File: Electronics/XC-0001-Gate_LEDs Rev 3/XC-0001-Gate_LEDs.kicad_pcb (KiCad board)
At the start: 2 copper layers, 76 x 60 mm, 16 parts, among them J1 DC12V_IN, J2 BuckBlock_NP, J3 LED_DIM, J4 LED_NODIM, J5 AC_IN, J6 AC_OUT

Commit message: Version 2 updates
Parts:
- removed JP1: Squelch_NO, Connector_Wire:SolderWire-0.25sqmm_1x02_P4.2mm_D0.65mm_OD1.7mm
- added C1: 22µF, Capacitor_SMD:C_1206_3216Metric_Pad1.33x1.80mm_HandSolder, B.Cu at (142.0, 121.0)
- added C2: 4.8µF, Capacitor_SMD:C_1206_3216Metric_Pad1.33x1.80mm_HandSolder, F.Cu at (147.8, 106.5)
- added C3: 10µF, Capacitor_SMD:C_1206_3216Metric_Pad1.33x1.80mm_HandSolder, F.Cu at (144.0, 106.5)
- added J7: Dim_Select, Connector_PinHeader_2.54mm:PinHeader_1x04_P2.54mm_Vertical, F.Cu at (138.0, 117.7)
- added L1: 68µH, Inductor_THT:L_Radial_D9.5mm_P5.00mm_Fastron_07HVP, F.Cu at (132.5, 102.0)
- added U1: LDU1416S1000, XC-footprint-lib:LDU1416S1000, F.Cu at (140.7, 93.0)
- J1, J3, J4: footprint Connector_Wire:SolderWire-0.25sqmm_1x02_P4.2mm_D0.65mm_OD1.7mm -> Connector_Wire:SolderWire-1.5sqmm_1x02_P7.8mm_D1.7mm_OD3.9mm
- J2: value BuckBlock_NP -> Driver_Ext; footprint Connector_Wire:SolderWire-1sqmm_1x06_P7.8mm_D1.4mm_OD3.9mm -> XC-footprint-lib:SolderWire-1.5sqmm_1x06_Grouped2x3_P6mm_D1.7mm_OD3mm
- J5, J6: footprint Connector_Wire:SolderWire-0.75sqmm_1x02_P7mm_D1.25mm_OD3.5mm -> Connector_Wire:SolderWire-1.5sqmm_1x02_P7.8mm_D1.7mm_OD3.9mm
- moved J2 24.8 mm to (164.5, 115.5)
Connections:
- net +12V renamed DC+12V
- net /LED+ renamed /DIM+
- net /LED- renamed /DIM-
- J2 pad 2: /DIM_ANALOG -> /DIM_CTRL
- RV1 pad 2: /DIM_ANALOG -> Net-(J7-Pad4)
- RV1 pad 3: /DIM_ANALOG -> Net-(J7-Pad4)
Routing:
- net /DIM_CTRL: track 0.00 -> 57.1 mm
- net /DIM+: track 19.8 -> 55.0 mm
- net /DIM-: track 8.24 -> 42.0 mm
- net /DIM_ANALOG: track 30.4 -> 0.00 mm
- net /DIM_GND: track 36.9 -> 54.9 mm
- net Net-(J7-Pad4): track 0.00 -> 16.5 mm
- net DC+12V: track 49.9 -> 64.9 mm, vias 0 -> 1
- net NEUT: track 26.0 -> 27.7 mm
- net DC-12V: vias 77 -> 112
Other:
- board size 76 x 60 mm -> 92 x 60 mm
- net class AC removed
- net class DC Pwr removed
- net class Default removed
- board text added: "+12V"
- board text added: "DIM"
- board text added: "Dim Pot"
- board text added: "Ext. Driver"
- board text added: "J7 Dim_Select Jumper: 4+3 → RV1 dimmer control 3+2 → Squelch (Full Dim) 2+1 → Disable (No Dim)"
- board text added: "Out"
- board text added: "Power"
- board text added: "RAC01-12SGB"
- board text added: "RV1 Dim Pot: A009 Offboard → 20KΩ LDU14 Onboard → 2MΩ"
- board text added: "XC-0001 Gate LED Control 3 04-2021"
- board text removed: "BuckBlock A009"
- board text removed: "Dim"
- board text removed: "Squelch (NO)"
- board text removed: "XC-0001 Gate LED Control 2 03-2021"

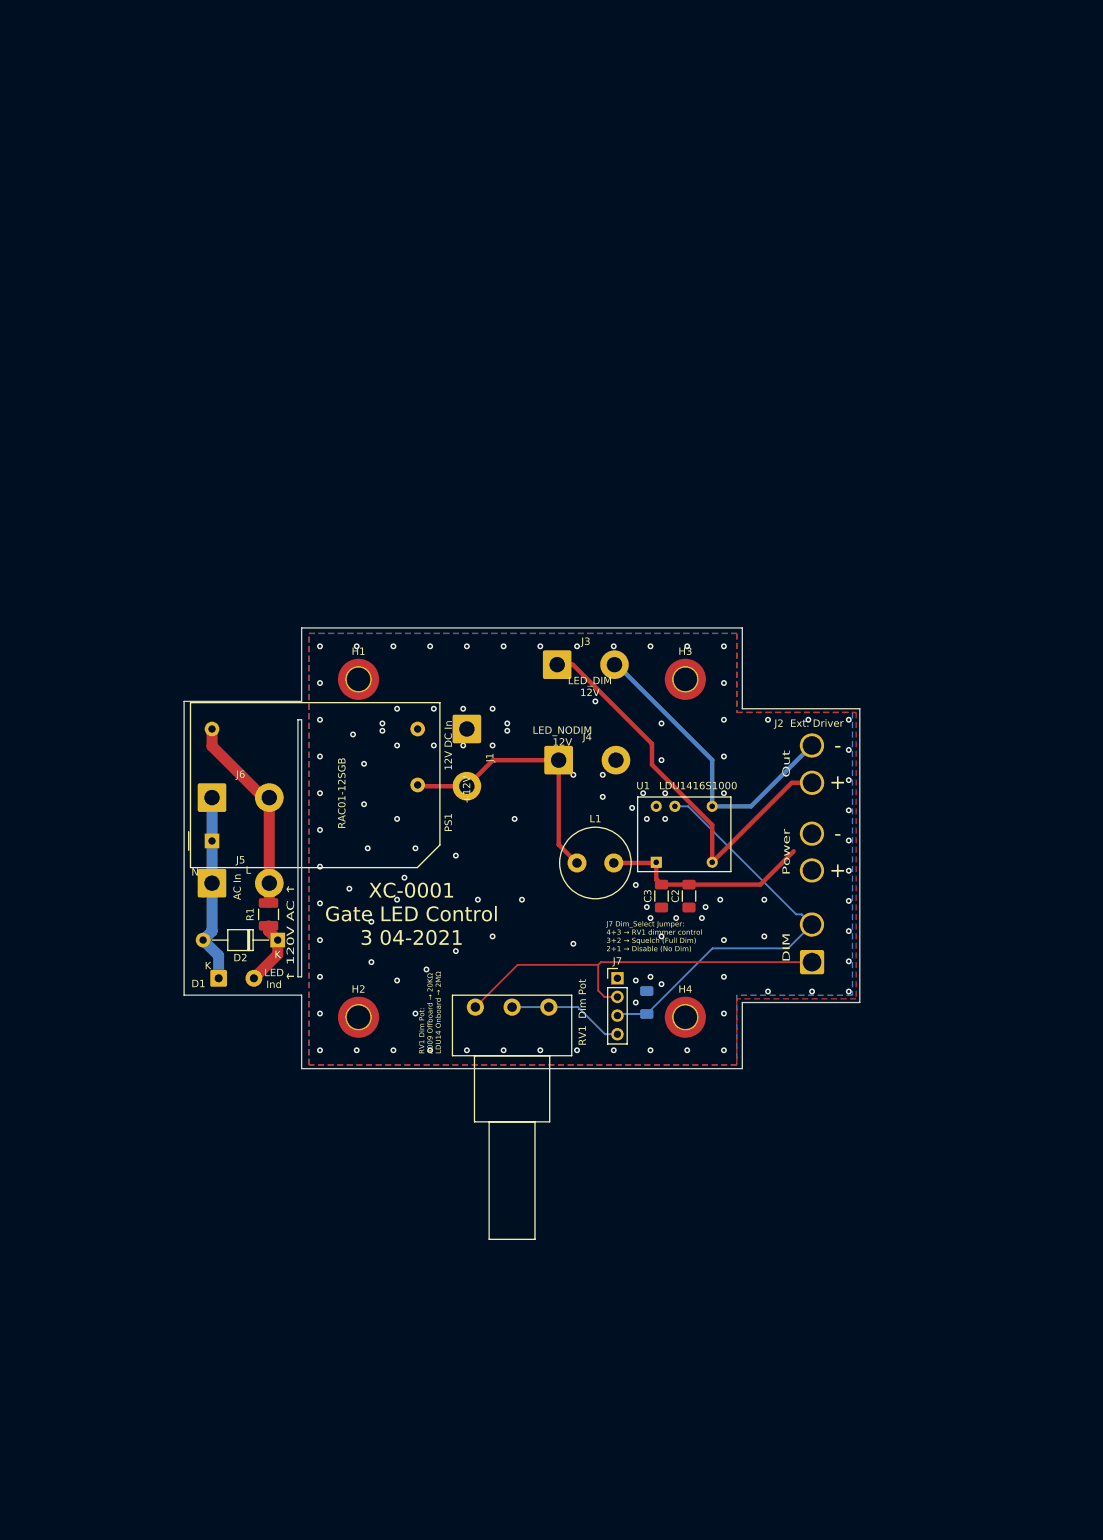
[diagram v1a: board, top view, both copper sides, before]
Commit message: Ignore backup
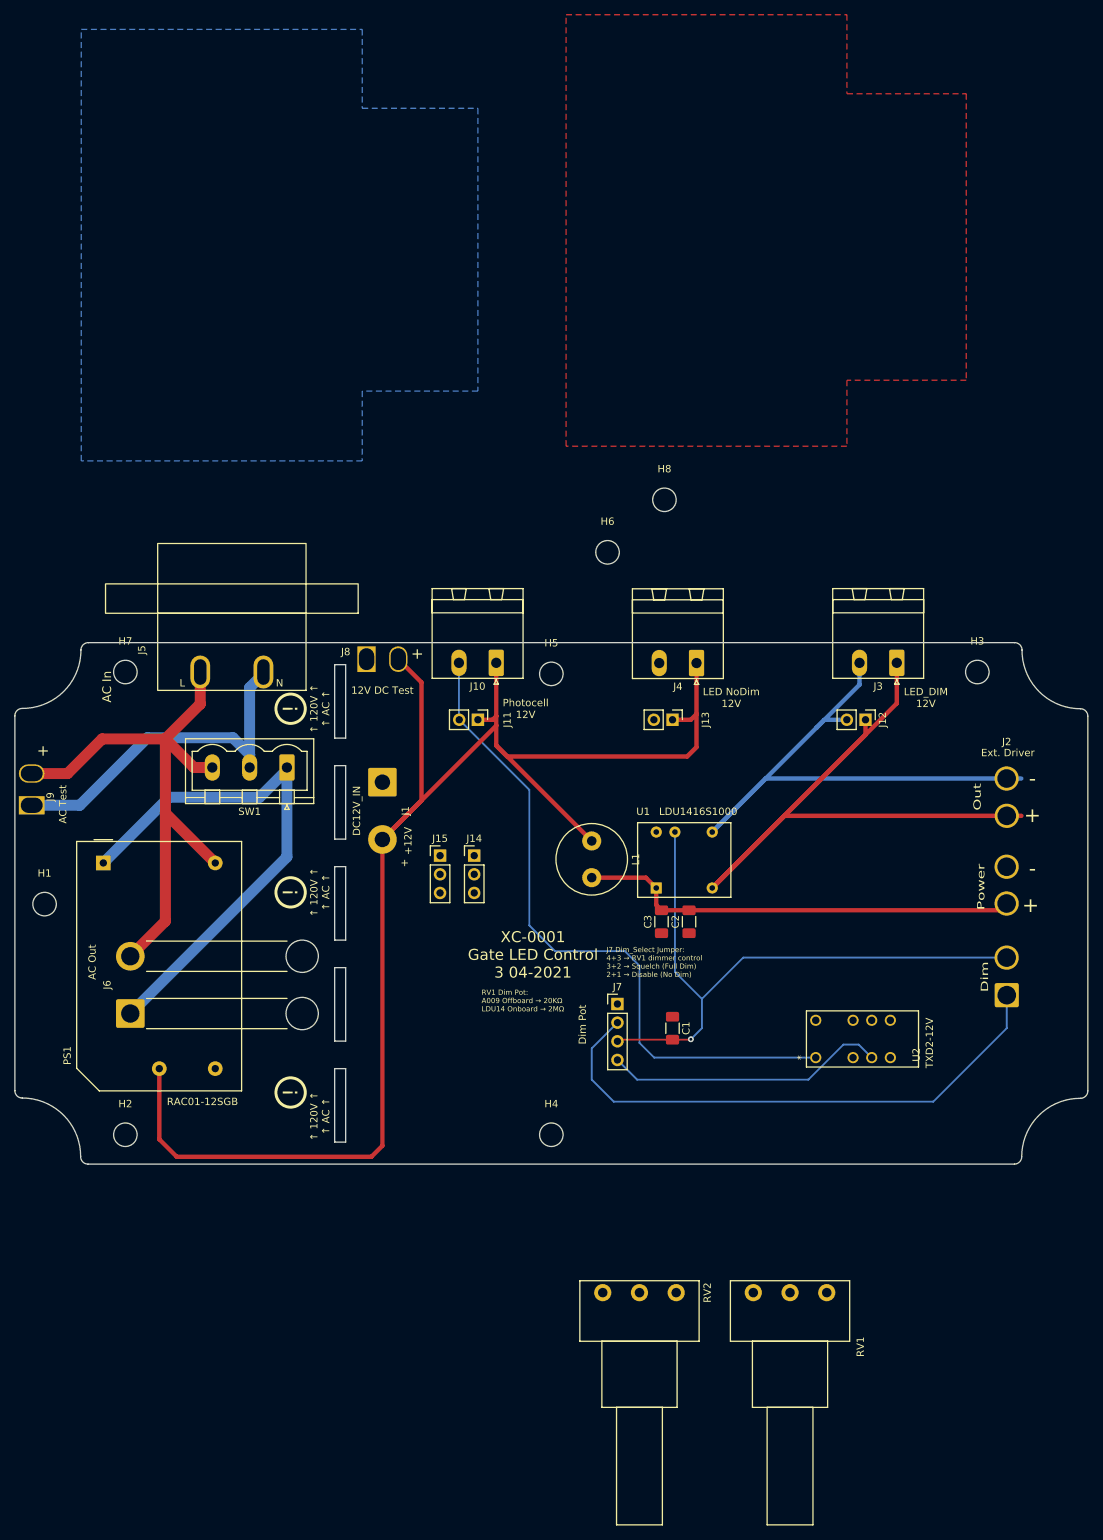
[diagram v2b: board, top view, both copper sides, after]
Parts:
- removed D1: LED, Connector_Wire:SolderWire-0.5sqmm_1x02_P4.8mm_D0.9mm_OD2.3mm
- removed D2: DIODE, Diode_THT:D_T-1_P10.16mm_Horizontal
- removed R1: 3kΩ, Resistor_SMD:R_1210_3225Metric_Pad1.30x2.65mm_HandSolder
- added H5: MountingHole, MountingHole:MountingHole_3.2mm_M3, F.Cu at (129.0, 76.2)
- added H6: MountingHole, MountingHole:MountingHole_3.2mm_M3, F.Cu at (136.7, 59.7)
- added H7: MountingHole, MountingHole:MountingHole_3.2mm_M3, F.Cu at (71.0, 76.0)
- added H8: MountingHole, MountingHole:MountingHole_3.2mm_M3, F.Cu at (144.4, 52.5)
- added J10: Photocell, Connector_Phoenix_MSTB:PhoenixContact_MSTBA_2,5_2-G-5,08_1x02_P5.08mm_Horizontal, F.Cu at (121.5, 74.8)
- added J11: Photocell_Pin, Connector_PinHeader_2.54mm:PinHeader_1x02_P2.54mm_Vertical, F.Cu at (119.0, 82.5)
- added J12: LED_Dim_Pin, Connector_PinHeader_2.54mm:PinHeader_1x02_P2.54mm_Vertical, F.Cu at (171.8, 82.5)
- added J13: LED_NoDim_Pin, Connector_PinHeader_2.54mm:PinHeader_1x02_P2.54mm_Vertical, F.Cu at (145.5, 82.5)
- added J14: Main PCB V, Connector_PinHeader_2.54mm:PinHeader_1x03_P2.54mm_Vertical, F.Cu at (118.5, 101.0)
- added J15: Pot PCB H, Connector_PinHeader_2.54mm:PinHeader_1x03_P2.54mm_Vertical, F.Cu at (113.8, 101.0)
- added J8: DC12V_Test, XC-footprint-lib:Test Holes, F.Cu at (106.0, 74.2)
- added J9: AC_Test, XC-footprint-lib:Test Holes, F.Cu at (58.2, 92.0)
- added RV2: Day_Dim, Potentiometer_THT:Potentiometer_Piher_PC-16_Single_Horizontal, F.Cu at (136.0, 160.5)
- added SW1: SW_SPST_LED, Connector_Phoenix_MSTB:PhoenixContact_MSTBVA_2,5_3-G-5,08_1x03_P5.08mm_Vertical, F.Cu at (93.0, 89.0)
- added U2: TXD2-12V, XC-footprint-lib:TXD2-12V, F.Cu at (165.0, 128.5)
- C1: moved to F.Cu
- H1, H2, H3, H4: footprint MountingHole:MountingHole_3.2mm_M3_DIN965_Pad_TopOnly -> MountingHole:MountingHole_3.2mm_M3
- J3: footprint Connector_Wire:SolderWire-1.5sqmm_1x02_P7.8mm_D1.7mm_OD3.9mm -> Connector_Phoenix_MSTB:PhoenixContact_MSTBA_2,5_2-G-5,08_1x02_P5.08mm_Horizontal
- J4: value LED_NODIM -> LED_NoDim; footprint Connector_Wire:SolderWire-1.5sqmm_1x02_P7.8mm_D1.7mm_OD3.9mm -> Connector_Phoenix_MSTB:PhoenixContact_MSTBA_2,5_2-G-5,08_1x02_P5.08mm_Horizontal
- J5: footprint Connector_Wire:SolderWire-1.5sqmm_1x02_P7.8mm_D1.7mm_OD3.9mm -> XC-footprint-lib:6160.0015 C8 Inlet (panel mount, PCB pins)
- J6: footprint Connector_Wire:SolderWire-1.5sqmm_1x02_P7.8mm_D1.7mm_OD3.9mm -> Connector_Wire:SolderWire-2sqmm_1x02_P7.8mm_D2mm_OD3.9mm_Relief
- RV1: value DIM_POT -> Night_Dim
- moved RV1 54.3 mm to (156.5, 160.5)
- moved H1 52.6 mm to (60.0, 107.6)
- moved J3 46.2 mm to (176.0, 74.8), turned to 180 degrees
- moved H3 39.8 mm to (187.0, 76.0)
- moved H2 35.6 mm to (71.0, 139.0)
- moved J6 31.4 mm to (71.7, 122.5), turned to 90 degrees
- moved J5 28.9 mm to (85.5, 76.0), turned to 180 degrees
- moved J2 26.9 mm to (191.0, 120.0)
- moved H4 24.3 mm to (129.0, 139.0)
- moved J4 23.0 mm to (148.8, 74.8), turned to 180 degrees
- moved PS1 15.1 mm to (68.0, 102.0), turned to -90 degrees
- moved J1 13.6 mm to (106.0, 91.0)
- moved C1 4.95 mm to (145.5, 124.5)
- moved L1 3.61 mm to (134.5, 99.0), turned to -90 degrees
- moved C2 3.50 mm to (147.8, 110.0)
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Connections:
- net DC-12V renamed DC-GND
- J6 pad 1: NEUT -> (no net)
- J7 pad 4: Net-(J7-Pad4) -> Dim_Ctrl_Out
- L1 pad 2: DC+12V -> /Driver+12V_In
- RV1 pad 1: /DIM_GND -> (no net)
- RV1 pad 2: Net-(J7-Pad4) -> Net-(RV1-Pad2)
- RV1 pad 3: Net-(J7-Pad4) -> Net-(RV1-Pad2)
- U1 pad 1: DC+12V -> /Driver+12V_In
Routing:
- net DC+12V: track 64.9 -> 259.9 mm, vias 1 -> 0
- net NEUT: track 27.7 -> 122.6 mm
- net Net-(J10-Pad2): track 0.00 -> 92.3 mm
- net /DIM+: track 55.0 -> 118.8 mm
- net LINE: track 26.6 -> 80.2 mm
- net /DIM-: track 42.0 -> 81.0 mm
- net Dim_Ctrl_Out: track 0.00 -> 38.4 mm
- net /DIM_CTRL: track 57.1 -> 84.7 mm, vias 0 -> 1
- net /DIM_GND: track 54.9 -> 75.6 mm
- net Net-(J7-Pad4): track 16.5 -> 0.00 mm
- net Net-(D1-Pad2): track 9.01 -> 0.00 mm
- net /Driver+12V_In: track 0.00 -> 8.57 mm
- net DC-GND: vias 112 -> 0
- added copper zone on B.Cu, net (none)
- added copper zone on F.Cu, net (none)
- removed copper zone on B.Cu, net DC-GND
- removed copper zone on F.Cu, net DC-GND
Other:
- board size 92 x 60 mm -> 146.1 x 71 mm
- board text added: "!"
- board text added: "12V DC Test"
- board text added: "AC Out"
- board text added: "AC Test"
- board text added: "Dim"
- board text added: "LED NoDim 12V"
- board text added: "Photocell 12V"
- board text added: "↑ 120V ↑ ↑ AC ↑"
- board text removed: "12V DC In"
- board text removed: "DIM"
- board text removed: "K"
- board text removed: "L"
- board text removed: "LED Ind"
- board text removed: "LED_NODIM 12V"
- board text removed: "Line"
- board text removed: "N"
- board text removed: "Neut"
- board text removed: "↑ 120V AC ↑"

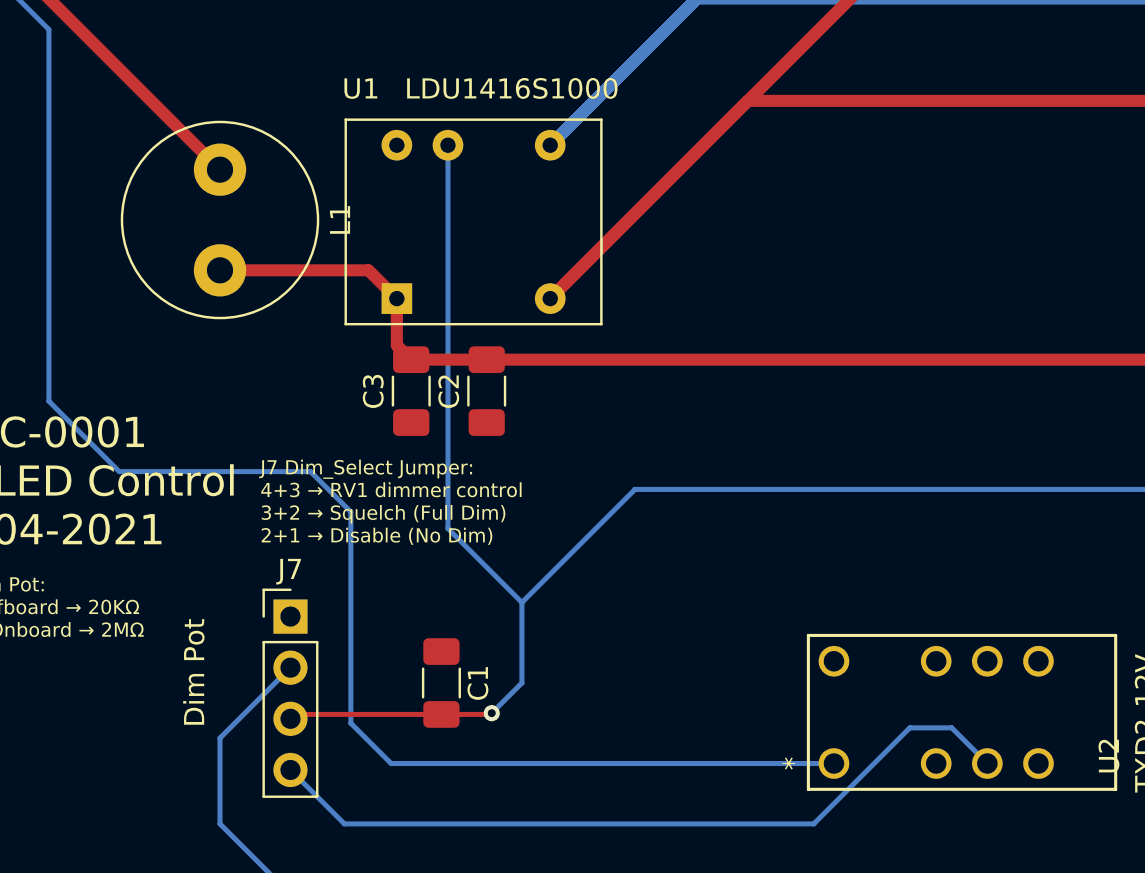
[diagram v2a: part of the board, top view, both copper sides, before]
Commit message: Remove inductor to debug false pin connection
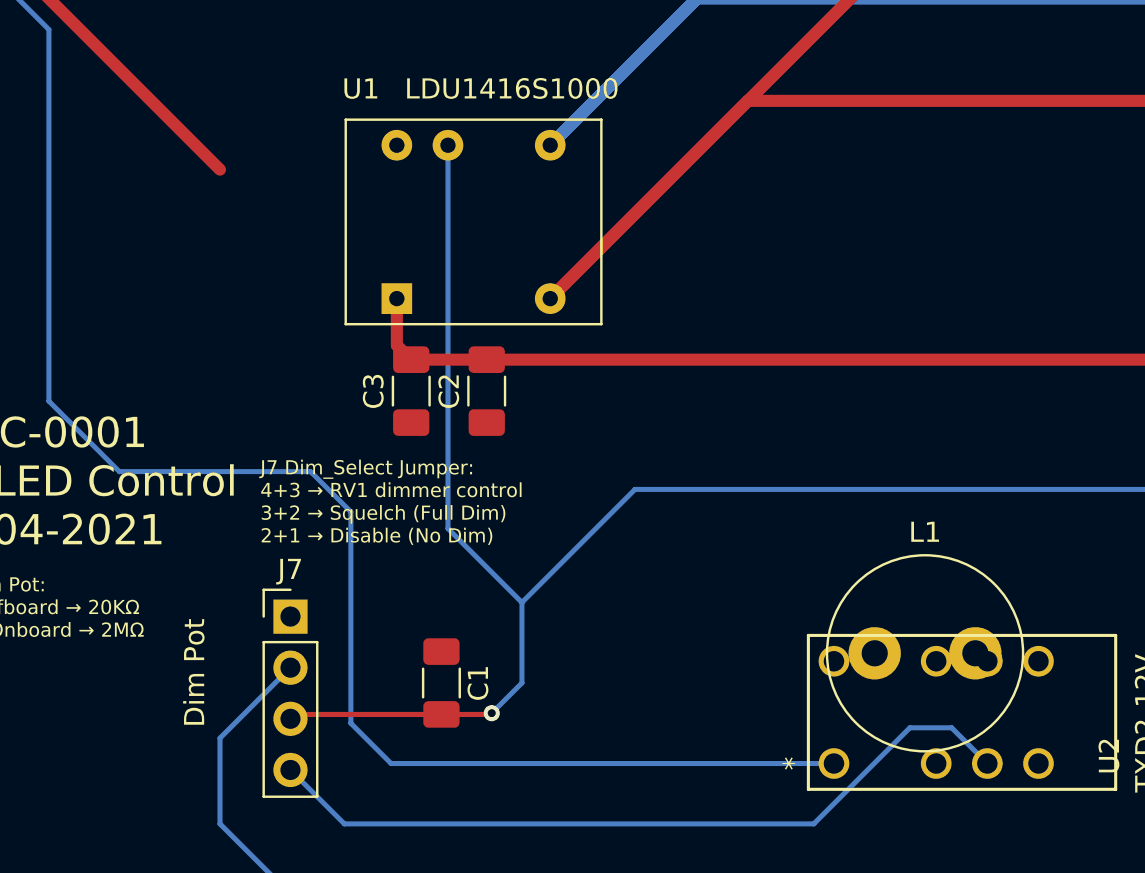
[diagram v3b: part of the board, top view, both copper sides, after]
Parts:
- moved L1 40.4 mm to (167.0, 123.0), turned to 0 degrees
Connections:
- J15 pad 1: (no net) -> Net-(RV1-Pad1)
- J15 pad 2: (no net) -> Net-(RV2-Pad2)
- J6 pad 1: (no net) -> Net-(J6-Pad1)
- L1 pad 2: /Driver+12V_In -> Net-(U1-Pad1)
- RV1 pad 1: (no net) -> Net-(RV1-Pad1)
- RV2 pad 1: (no net) -> Net-(RV1-Pad1)
- RV2 pad 2: (no net) -> Net-(RV2-Pad2)
- RV2 pad 3: (no net) -> Net-(RV2-Pad2)
- SW1 pad 1: (no net) -> Net-(J6-Pad1)
- U1 pad 1: /Driver+12V_In -> (no net)
- U2 pad 3: (no net) -> Day
- U2 pad 5: (no net) -> Night
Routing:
- net Net-(J6-Pad1): track 0.00 -> 72.9 mm
- net NEUT: track 122.6 -> 49.7 mm
- net /Driver+12V_In: track 8.57 -> 0.00 mm
